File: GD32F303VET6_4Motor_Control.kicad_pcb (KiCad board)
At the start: 6 copper layers, 100 x 60 mm, 156 parts, among them CN1 KF2EDGK-5.08-2P, CN4 WJ15EDGRC-3.81-2P, CN5 KF15EDGRC3.81-6P, CN6 KF15EDGRC3.81-6P, CN7 KF15EDGRC3.81-6P, CN8 KF15EDGRC3.81-6P, J1 TYPE-C-31-M-31, J2 TYPE-C 16PIN 2MD(073), Q16 CJ3134K KF, Q17 CJ3134K KF, Q3 CJ3134K, SW1 SKRPACE010, U1 XL1509-5.0, U13 SIT3485ESA, U15 TXS0104EPWR, U19 CH340N, U20 LM66100DCKR, U21 LM66100DCKR, U22 SN74LVC2G06DBVR, U23 SN74LVC2G06DBVR, U24 SN74LVC2G06DBVR, U25 SN74LVC2G06DBVR, U5 LM66100DCKR, U6 SY8089A1AAC, U7 GD32F303VET6, U8 GD25Q16ESIGR, Y1 TAXM8M4RDBCCT2T, Y2 XKXGI-SUA-32.768K

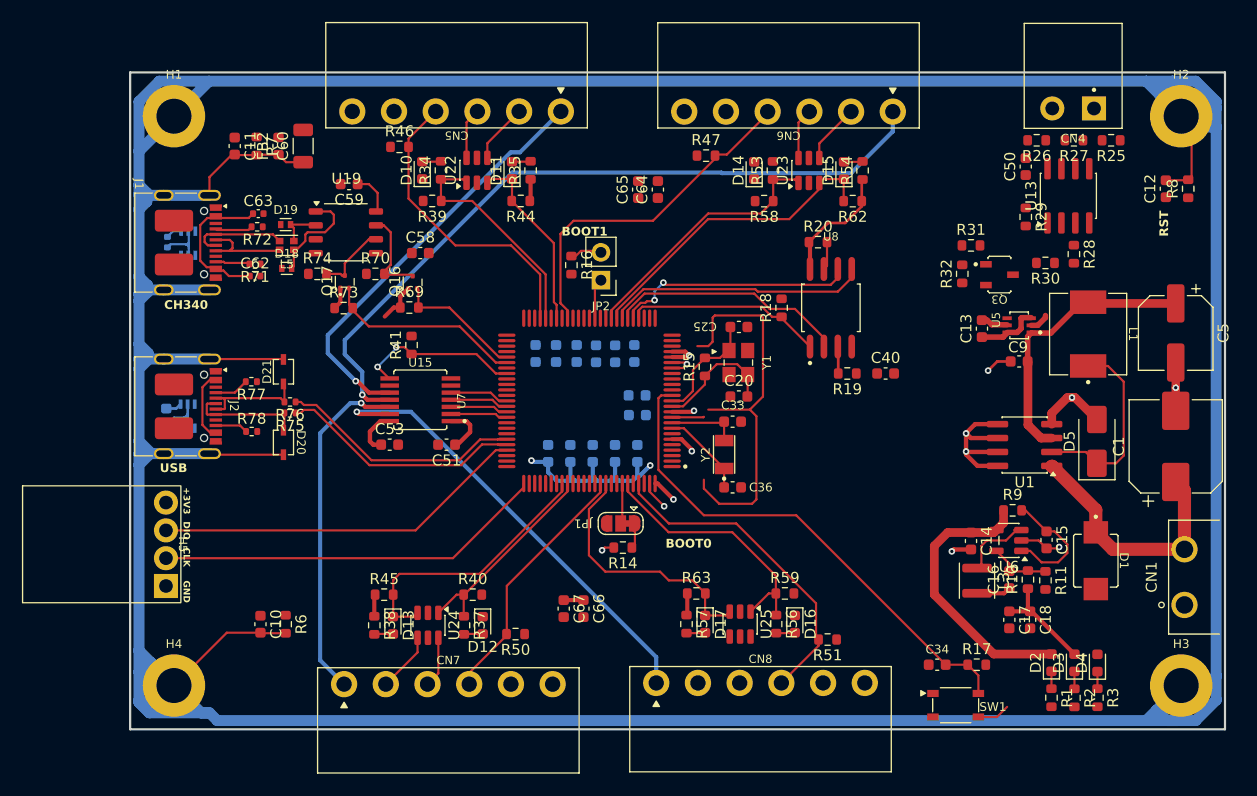
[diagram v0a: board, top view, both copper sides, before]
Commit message: 更新V2.0电路设计及0.5oz内层制造交付资料
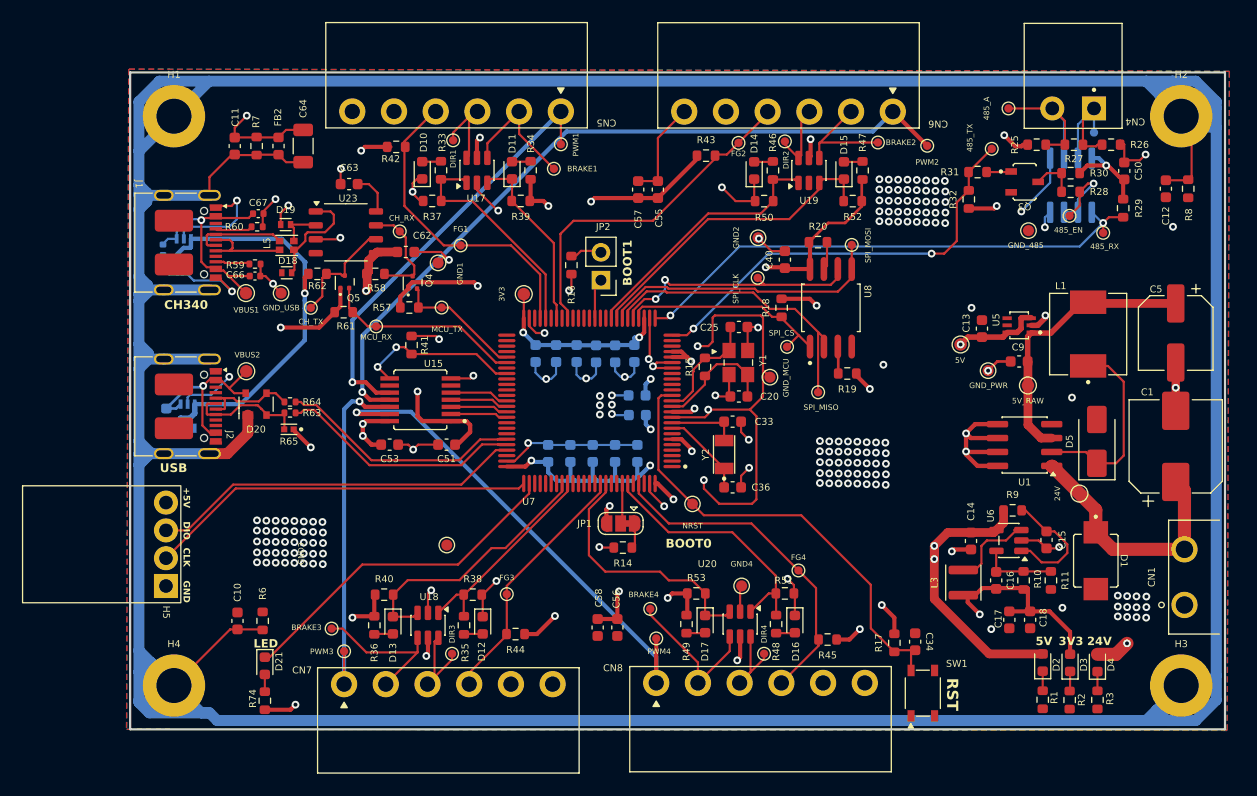
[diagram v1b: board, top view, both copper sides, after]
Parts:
- removed R77, R78: 0402WGF5101TCE, Resistor_SMD:R_0402_1005Metric
- added R65: 0402WGF1001TCE, kicad_api_lib:0402WGF1001TCE, F.Cu at (100.0, 91.6)
- added R74: 1k, Resistor_SMD:R_0603_1608Metric, F.Cu at (97.8, 116.4)
- added TP_24V1: 24V, kicad_api_lib:TestPoint_Pad_D1.143mm, F.Cu at (172.2, 97.5)
- added TP_3V3: 3V3, kicad_api_lib:TestPoint_Pad_D1.143mm, F.Cu at (121.5, 79.2)
- added TP_485_A1: 485_A, kicad_api_lib:TestPoint_Pad_D0.762mm, F.Cu at (165.7, 62.3)
- added TP_485_B1: 485_B, kicad_api_lib:TestPoint_Pad_D0.762mm, B.Cu at (173.5, 64.5)
- added TP_485_EN1: 485_EN, kicad_api_lib:TestPoint_Pad_D0.762mm, F.Cu at (171.3, 72.1)
- added TP_485_RX1: 485_RX, kicad_api_lib:TestPoint_Pad_D0.762mm, F.Cu at (174.4, 73.7)
- added TP_485_TX1: 485_TX, kicad_api_lib:TestPoint_Pad_D0.762mm, F.Cu at (164.2, 66.0)
- added TP_5V1: 5V, kicad_api_lib:TestPoint_Pad_D1.143mm, F.Cu at (161.3, 83.8)
- added TP_5V_RAW1: 5V_RAW, kicad_api_lib:TestPoint_Pad_D1.143mm, F.Cu at (167.5, 87.6)
- added TP_BRAKE1: BRAKE1, kicad_api_lib:TestPoint_Pad_D0.762mm, F.Cu at (124.2, 67.8)
- added TP_BRAKE2: BRAKE2, kicad_api_lib:TestPoint_Pad_D0.762mm, F.Cu at (153.8, 65.4)
- added TP_BRAKE3: BRAKE3, kicad_api_lib:TestPoint_Pad_D0.762mm, F.Cu at (103.9, 109.8)
- added TP_BRAKE4: BRAKE4, kicad_api_lib:TestPoint_Pad_D0.762mm, F.Cu at (133.0, 108.0)
- added TP_CH_RX1: CH_RX, kicad_api_lib:TestPoint_Pad_D0.762mm, F.Cu at (110.1, 73.5)
- added TP_CH_TX1: CH_TX, kicad_api_lib:TestPoint_Pad_D0.762mm, F.Cu at (102.0, 80.5)
- added TP_DIR1: DIR1, kicad_api_lib:TestPoint_Pad_D0.762mm, F.Cu at (115.0, 65.2)
- added TP_DIR2: DIR2, kicad_api_lib:TestPoint_Pad_D0.762mm, F.Cu at (145.3, 65.3)
- added TP_DIR3: DIR3, kicad_api_lib:TestPoint_Pad_D0.762mm, F.Cu at (114.9, 112.1)
- added TP_DIR4: DIR4, kicad_api_lib:TestPoint_Pad_D0.762mm, F.Cu at (143.4, 112.1)
- added TP_FG1: FG1, kicad_api_lib:TestPoint_Pad_D0.762mm, F.Cu at (115.7, 74.8)
- added TP_FG2: FG2, kicad_api_lib:TestPoint_Pad_D0.762mm, F.Cu at (141.1, 65.4)
- added TP_FG3: FG3, kicad_api_lib:TestPoint_Pad_D0.762mm, F.Cu at (119.9, 106.7)
- added TP_FG4: FG4, kicad_api_lib:TestPoint_Pad_D0.762mm, F.Cu at (146.5, 104.5)
- added TP_GND1: GND1, kicad_api_lib:TestPoint_Pad_D1.016mm, F.Cu at (113.6, 76.4)
- added TP_GND2: GND2, kicad_api_lib:TestPoint_Pad_D1.016mm, F.Cu at (142.8, 74.1)
- added TP_GND3: GND3, kicad_api_lib:TestPoint_Pad_D1.016mm, F.Cu at (114.4, 102.2)
- added TP_GND4: GND4, kicad_api_lib:TestPoint_Pad_D1.016mm, F.Cu at (141.3, 105.9)
- added TP_GND_485: GND_485, kicad_api_lib:TestPoint_Pad_D1.016mm, F.Cu at (167.6, 73.5)
- added TP_GND_MCU1: GND_MCU, kicad_api_lib:TestPoint_Pad_D1.016mm, F.Cu at (143.9, 86.8)
- added TP_GND_PWR1: GND_PWR, kicad_api_lib:TestPoint_Pad_D1.016mm, F.Cu at (163.9, 86.2)
- added TP_GND_USB1: GND_USB, kicad_api_lib:TestPoint_Pad_D1.016mm, F.Cu at (99.3, 79.2)
- added TP_MCU_RX1: MCU_RX, kicad_api_lib:TestPoint_Pad_D0.762mm, F.Cu at (108.0, 82.2)
- added TP_MCU_TX1: MCU_TX, kicad_api_lib:TestPoint_Pad_D0.762mm, F.Cu at (113.9, 80.5)
- added TP_NRST1: NRST, TestPoint:TestPoint_Pad_D1.0mm, F.Cu at (136.9, 98.4)
- added TP_PWM1: PWM1, kicad_api_lib:TestPoint_Pad_D0.762mm, F.Cu at (124.8, 65.6)
- added TP_PWM2: PWM2, kicad_api_lib:TestPoint_Pad_D0.762mm, F.Cu at (158.3, 65.7)
- added TP_PWM3: PWM3, kicad_api_lib:TestPoint_Pad_D0.762mm, F.Cu at (105.0, 111.9)
- added TP_PWM4: PWM4, kicad_api_lib:TestPoint_Pad_D0.762mm, F.Cu at (133.6, 110.7)
- added TP_SPI_CLK1: SPI_CLK, kicad_api_lib:TestPoint_Pad_D0.762mm, F.Cu at (142.8, 77.8)
- added TP_SPI_CS1: SPI_CS, kicad_api_lib:TestPoint_Pad_D0.762mm, F.Cu at (145.5, 84.1)
- added TP_SPI_MISO1: SPI_MISO, kicad_api_lib:TestPoint_Pad_D0.762mm, F.Cu at (148.3, 88.2)
- added TP_SPI_MOSI1: SPI_MOSI, kicad_api_lib:TestPoint_Pad_D0.762mm, F.Cu at (151.4, 74.8)
- added TP_VBUS1: VBUS1, kicad_api_lib:TestPoint_Pad_D1.143mm, F.Cu at (96.1, 79.2)
- added TP_VBUS2: VBUS2, kicad_api_lib:TestPoint_Pad_D1.143mm, F.Cu at (96.1, 86.3)
- D20: value SD03C -> PRTR5V0U2X; footprint kicad_api_lib:SD03C -> kicad_api_lib:PRTR5V0U2X
- D21: value SD03C -> STATUS_GREEN; footprint kicad_api_lib:SD03C -> LED_SMD:LED_0603_1608Metric
- U13: moved to B.Cu
- moved D21 26.9 mm to (97.8, 113.2), turned to -90 degrees
- moved C40 13.9 mm to (145.3, 76.1), turned to 90 degrees
- moved C50 9.01 mm to (176.3, 68.0)
- moved R29 8.94 mm to (176.2, 71.4)
- moved Q3 8.78 mm to (167.2, 69.0)
- moved R30 8.52 mm to (171.4, 68.2), turned to 0 degrees
- moved R17 7.79 mm to (155.3, 111.1), turned to 90 degrees
- moved R32 6.83 mm to (162.1, 70.6)
- moved R25 6.81 mm to (168.3, 65.6), turned to 0 degrees
- moved R26 6.81 mm to (175.1, 65.6), turned to 0 degrees
- moved R31 6.73 mm to (162.9, 68.1)
- moved R28 5.71 mm to (171.4, 69.9), turned to 180 degrees
- moved D20 4.30 mm to (97.0, 89.3)
- moved C56 3.55 mm to (130.0, 109.7)
- moved C58 3.55 mm to (128.2, 109.7)
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- renumbered C64 to C55, C66 to C56, C65 to C57, C67 to C58, C57 to C61, C58 to C62, C59 to C63, C60 to C64, C61 to C65, C62 to C66, C63 to C67, Q16 to Q4, Q17 to Q5, R34 to R33, R35 to R34, R37 to R35, R38 to R36, R39 to R37, R40 to R38, R44 to R39, R45 to R40, R46 to R42, R47 to R43, R50 to R44, R51 to R45, R53 to R46, R54 to R47, R56 to R48, R57 to R49, R58 to R50, R59 to R51, R62 to R52, R63 to R53, R69 to R57, R70 to R58, R71 to R59, R72 to R60, R73 to R61, R74 to R62, R75 to R63, R76 to R64, U22 to U17, U24 to U18, U23 to U19, U25 to U20, U19 to U23, U20 to U24, U21 to U25
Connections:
- net /MCU_Core/USART0_RX renamed /MCU_Core/USART2_RX
- net /MCU_Core/USART0_TX renamed /MCU_Core/USART2_TX
- net Net-(U13-DE) renamed /RS485/RS485_EN
- D21 pad 1: /MCU_Core/USB_TTL_CH340/DN2 -> /MCU_Core/LED_PA15_N
- D21 pad 2: Earth -> Net-(D21-A)
- J2 pad A5: Net-(J2-CC1) -> unconnected-(J2-CC1-PadA5)
- J2 pad B5: Net-(J2-CC2) -> unconnected-(J2-CC2-PadB5)
- U7 pad 77: unconnected-(U7C-PA15-Pad77) -> /MCU_Core/LED_PA15_N
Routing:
- net GND: track 60.4 -> 234.4 mm, vias 10 -> 191
- net +5V: track 35.8 -> 181.8 mm, vias 0 -> 7
- net +3V3: track 73.3 -> 188.3 mm, vias 6 -> 36
- net /RS485/RS485_RX: track 0.00 -> 48.9 mm, vias 0 -> 2
- net /RS485/RS485_TX: track 0.00 -> 39.4 mm, vias 0 -> 2
- net (no net): track 36.0 -> 0.00 mm
- net /MCU_Core/LED_PA15_N: track 0.00 -> 31.2 mm
- net /RS485/RS485A: track 0.00 -> 14.1 mm
- net /MCU_Core/Motor_Comm/MOTOR_BRAKE4: track 0.00 -> 14.0 mm
- net /RS485/RS485B: track 0.00 -> 12.9 mm
- net USB2_VBUS: track 8.04 -> 17.8 mm, vias 0 -> 1
- net Earth: track 440.9 -> 431.3 mm
- net /MCU_Core/Motor_Comm/MOTOR_BRAKE3: track 5.44 -> 14.2 mm
- net /RS485/RS485_EN: track 0.00 -> 8.73 mm, vias 0 -> 1
- net /MCU_Core/Motor_Comm/MOTOR_DIR4: track 0.00 -> 8.24 mm
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- added copper zone on In2.Cu, net +24V
- added copper zone on In3.Cu, net +3V3
- added copper zone on In3.Cu, net +5V
- added copper zone on B.Cu, net GND
- added copper zone on F.Cu, net GND
- added copper zone on In1.Cu, net GND
- added copper zone on In4.Cu, net GND
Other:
- board text added: "+5V"
- board text added: "24V"
- board text added: "3V3"
- board text added: "5V"
- board text added: "LED"
- board text removed: "+3V3"
